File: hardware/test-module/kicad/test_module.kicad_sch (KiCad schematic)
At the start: 16 parts, among them J1 Barrel_Jack_12V, J2 Scale_Molex_43645, M1 ERM_Motor, M2 Stepper_4wire, M3 Servo_3pin, U1 D24V22F5_Buck, U2 Pi_Pico_W, U3 DRV2605L_Breakout, U4 DRV8871_Breakout, U5 Tic_T500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

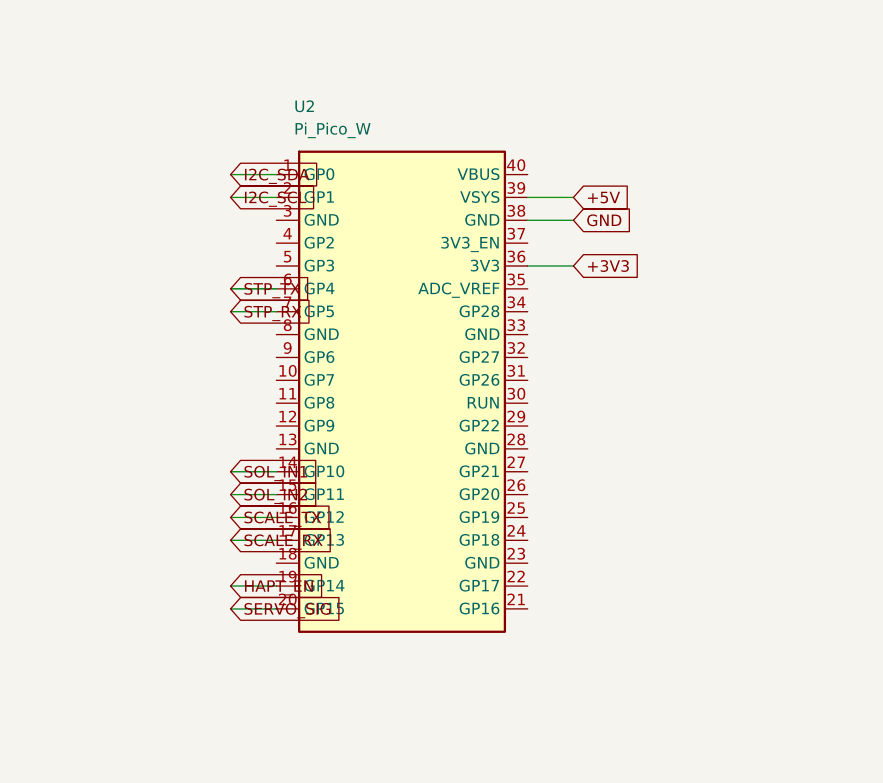
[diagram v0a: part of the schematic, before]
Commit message: fix review feedback in scale and kicad generation
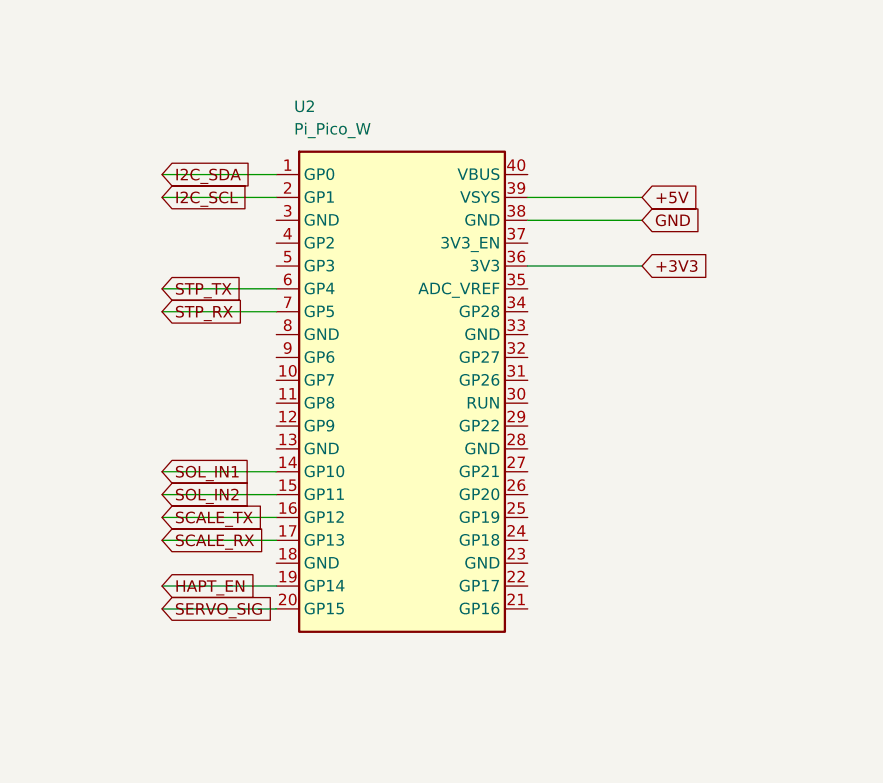
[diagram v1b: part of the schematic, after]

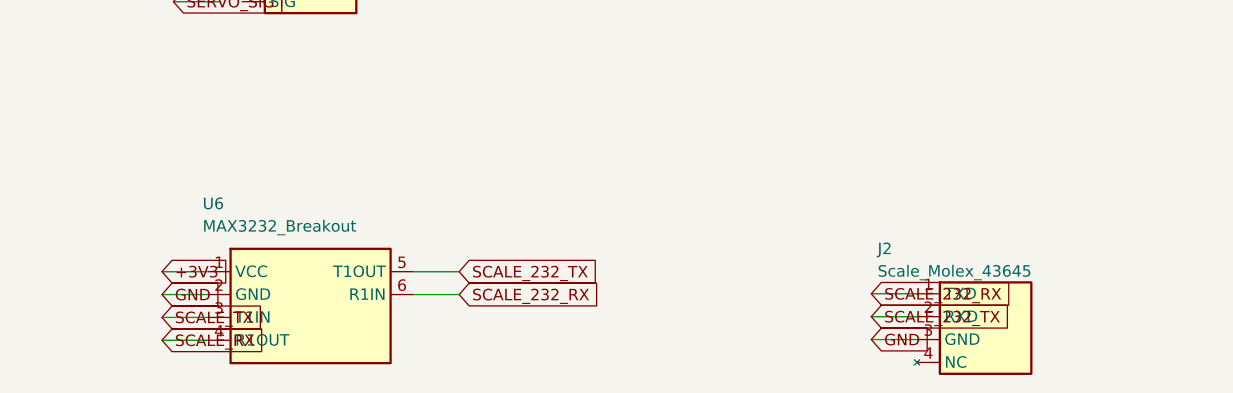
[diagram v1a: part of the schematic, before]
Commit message: Assume Waveshare Pico-2CH-RS232 module for the scale RS-232 link
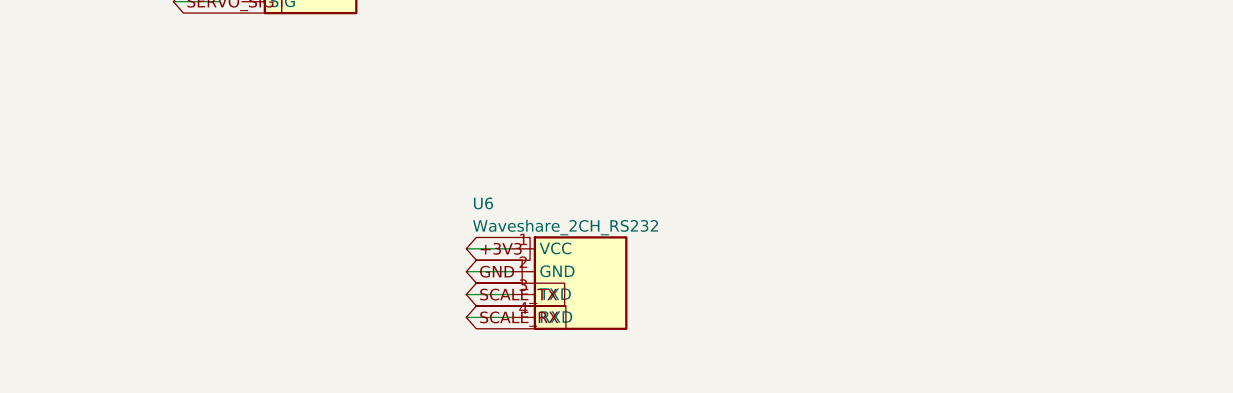
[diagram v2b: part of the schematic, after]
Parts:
- removed J2: Scale_Molex_43645, symbol test_module:Scale_Molex_43645
- removed U6: MAX3232_Breakout, symbol test_module:MAX3232_Breakout
- added U6: Waveshare_2CH_RS232, symbol test_module:Waveshare_2CH_RS232
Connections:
- net +3V3: now also U6.1 (VCC)
- net GND: now also U6.2 (GND)
- net SCALE_RX: now also U6.4 (RXD)
- net SCALE_TX: now also U6.3 (TXD)
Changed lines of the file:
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@@
   (comment 1 "Exercises auger stepper + ERM vibration + tap solenoid + dispense-angle servo")
   (comment 2 "Resolves issue #50; parts from PR #25")
-  (comment 3 "Rev B: A&D HR-100A scale feedback via MAX3232 RS-232 on UART0 (issue #99)")
+  (comment 3 "Rev B: A&D HR-100A scale feedback via Waveshare Pico-2CH-RS232 on UART0 (issue #99)")
   (comment 4 "")
 )
@@
   (effects (font (size 1.27 1.27)) (justify left))
 )
-(symbol (lib_id "test_module:MAX3232_Breakout") (at 210 245 0) (unit 1)
-  (in_bom yes) (on_board yes) (dnp no)
-  (property "Reference" "U6" (id 0) (at 198 240 0)
-    (effects (font (size 1.27 1.27)) (justify left)))
-  (property "Value" "MAX3232_Breakout" (id 1) (at 198 242.5 0)
-    (effects (font (size 1.27 1.27)) (justify left)))
-  (property "Footprint" "" (id 2) (at 210 245 0)
-    (effects (font (size 1.27 1.27)) hide))
-  (property "Datasheet" "" (id 3) (at 210 245 0)
+(symbol (lib_id "test_module:Waveshare_2CH_RS232") (at 240 245 0) (unit 1)
+  (in_bom yes) (on_board yes) (dnp no)
+  (property "Reference" "U6" (id 0) (at 228 240 0)
+    (effects (font (size 1.27 1.27)) (justify left)))
+  (property "Value" "Waveshare_2CH_RS232" (id 1) (at 228 242.5 0)
+    (effects (font (size 1.27 1.27)) (justify left)))
+  (property "Footprint" "" (id 2) (at 240 245 0)
+    (effects (font (size 1.27 1.27)) hide))
+  (property "Datasheet" "" (id 3) (at 240 245 0)
     (effects (font (size 1.27 1.27)) hide))
   (instances
@@
   )
 )
-(wire (pts (xy 198.57 247.54) (xy 193.48999999999998 247.54))
-  (stroke (width 0) (type default))
-)
-(global_label "+3V3" (shape input) (at 193.48999999999998 247.54 180) (fields_autoplaced)
-  (effects (font (size 1.27 1.27)) (justify left))
-)
-(wire (pts (xy 198.57 250.08) (xy 193.48999999999998 250.08))
-  (stroke (width 0) (type default))
-)
-(global_label "GND" (shape input) (at 193.48999999999998 250.08 180) (fields_autoplaced)
-  (effects (font (size 1.27 1.27)) (justify left))
-)
-(wire (pts (xy 198.57 252.62) (xy 193.48999999999998 252.62))
-  (stroke (width 0) (type default))
-)
-(global_label "SCALE_TX" (shape input) (at 193.48999999999998 252.62 180) (fields_autoplaced)
-  (effects (font (size 1.27 1.27)) (justify left))
-)
-(wire (pts (xy 198.57 255.16) (xy 193.48999999999998 255.16))
-  (stroke (width 0) (type default))
-)
-(global_label "SCALE_RX" (shape input) (at 193.48999999999998 255.16 180) (fields_autoplaced)
-  (effects (font (size 1.27 1.27)) (justify left))
-)
-(wire (pts (xy 221.43 247.54) (xy 226.51000000000002 247.54))
-  (stroke (width 0) (type default))
-)
-(global_label "SCALE_232_TX" (shape input) (at 226.51000000000002 247.54 0) (fields_autoplaced)
-  (effects (font (size 1.27 1.27)) (justify left))
-)
-(wire (pts (xy 221.43 250.08) (xy 226.51000000000002 250.08))
-  (stroke (width 0) (type default))
-)
-(global_label "SCALE_232_RX" (shape input) (at 226.51000000000002 250.08 0) (fields_autoplaced)
-  (effects (font (size 1.27 1.27)) (justify left))
-)
-(symbol (lib_id "test_module:Scale_Molex_43645") (at 285 250 0) (unit 1)
-  (in_bom yes) (on_board yes) (dnp no)
-  (property "Reference" "J2" (id 0) (at 273 245 0)
-    (effects (font (size 1.27 1.27)) (justify left)))
-  (property "Value" "Scale_Molex_43645" (id 1) (at 273 247.5 0)
-    (effects (font (size 1.27 1.27)) (justify left)))
-  (property "Footprint" "" (id 2) (at 285 250 0)
-    (effects (font (size 1.27 1.27)) hide))
-  (property "Datasheet" "" (id 3) (at 285 250 0)
-    (effects (font (size 1.27 1.27)) hide))
-  (instances
-    (project "test_module"
-      (path "/00000000-0000-0000-0002-000000000001"
-        (reference "J2") (unit 1)
-      )
-    )
-  )
-)
-(wire (pts (xy 277.38 250) (xy 272.3 250))
-  (stroke (width 0) (type default))
-)
-(global_label "SCALE_232_RX" (shape input) (at 272.3 250 180) (fields_autoplaced)
-  (effects (font (size 1.27 1.27)) (justify left))
-)
-(wire (pts (xy 277.38 252.54) (xy 272.3 252.54))
-  (stroke (width 0) (type default))
-)
-(global_label "SCALE_232_TX" (shape input) (at 272.3 252.54 180) (fields_autoplaced)
-  (effects (font (size 1.27 1.27)) (justify left))
-)
-(wire (pts (xy 277.38 255.08) (xy 272.3 255.08))
-  (stroke (width 0) (type default))
-)
-(global_label "GND" (shape input) (at 272.3 255.08 180) (fields_autoplaced)
-  (effects (font (size 1.27 1.27)) (justify left))
-)
+(wire (pts (xy 232.38 245) (xy 227.29999999999998 245))
+  (stroke (width 0) (type default))
+)
+(global_label "+3V3" (shape input) (at 227.29999999999998 245 180) (fields_autoplaced)
+  (effects (font (size 1.27 1.27)) (justify left))
+)
+(wire (pts (xy 232.38 247.54) (xy 227.29999999999998 247.54))
+  (stroke (width 0) (type default))
+)
+(global_label "GND" (shape input) (at 227.29999999999998 247.54 180) (fields_autoplaced)
+  (effects (font (size 1.27 1.27)) (justify left))
+)
+(wire (pts (xy 232.38 250.08) (xy 227.29999999999998 250.08))
+  (stroke (width 0) (type default))
+)
+(global_label "SCALE_TX" (shape input) (at 227.29999999999998 250.08 180) (fields_autoplaced)
+  (effects (font (size 1.27 1.27)) (justify left))
+)
+(wire (pts (xy 232.38 252.62) (xy 227.29999999999998 252.62))
+  (stroke (width 0) (type default))
+)
+(global_label "SCALE_RX" (shape input) (at 227.29999999999998 252.62 180) (fields_autoplaced)
+  (effects (font (size 1.27 1.27)) (justify left))
+)
